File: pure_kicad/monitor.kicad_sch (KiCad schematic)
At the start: 46 parts, among them J3 XT60M, J4 XT60M, J5 Conn_01x04_Pin, J6 Conn_01x04_Pin, Q5 Q_PMOS_SGD, Q6 Q_NMOS_DGS, Q7 Q_NMOS_DGS, U2 BQ40Z80RSMR

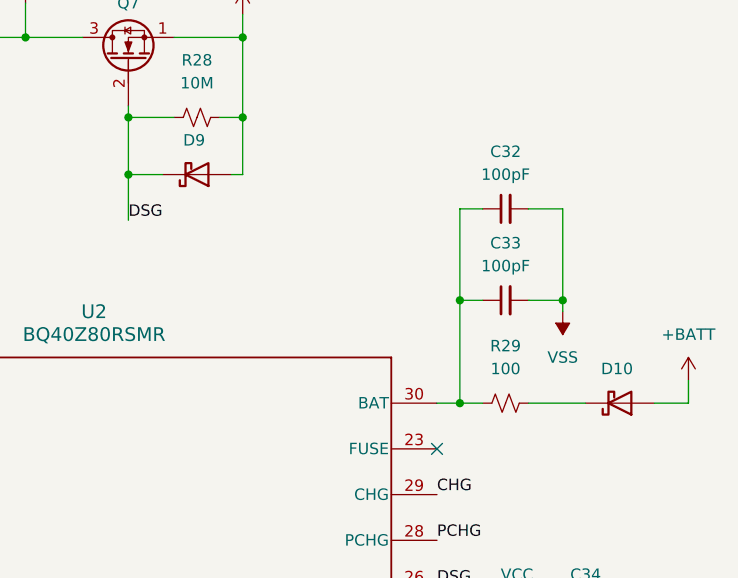
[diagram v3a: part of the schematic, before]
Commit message: So, 10u X5Rs are a thing. Just use 40 of them
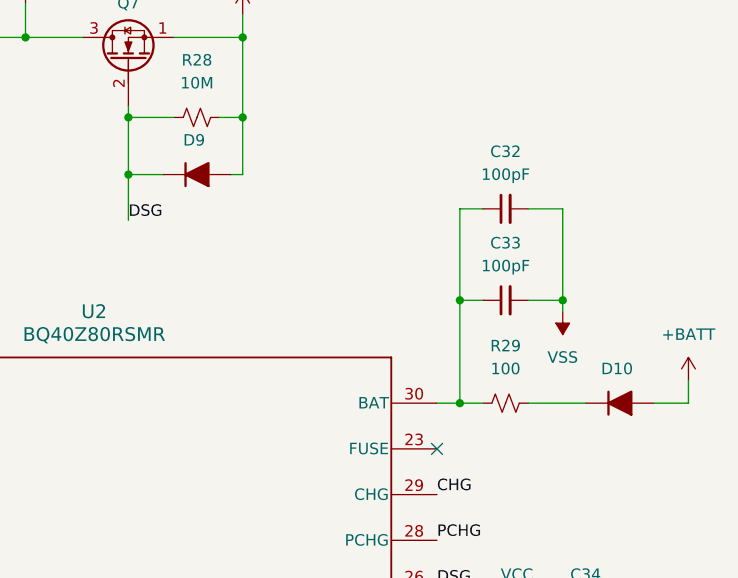
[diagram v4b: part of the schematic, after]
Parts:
- D10, D9: value D_Schottky -> 1N4001; footprint cyberec:D_SMA_Handsoldering -> cyberec:D_SOD-123F; symbol Device:D_Schottky -> Device:D_Filled
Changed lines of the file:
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@@
 	)
 	(symbol
-		(lib_id "Device:D_Schottky")
+		(lib_id "Device:D_Filled")
 		(at 173.99 48.26 0)
 		(mirror x)
@@
 			)
 		)
-		(property "Value" "D_Schottky"
+		(property "Value" "1N4001"
 			(at 173.6725 44.45 0)
 			(effects
@@
 			)
 		)
-		(property "Footprint" "cyberec:D_SMA_Handsoldering"
+		(property "Footprint" "cyberec:D_SOD-123F"
 			(at 173.99 48.26 0)
 			(effects
@@
 			)
 		)
-		(property "Description" "Schottky diode"
+		(property "Description" "Diode, filled shape"
+			(at 173.99 48.26 0)
+			(effects
+				(font
+					(size 1.27 1.27)
+				)
+				(hide yes)
+			)
+		)
+		(property "Sim.Device" "D"
+			(at 173.99 48.26 0)
+			(effects
+				(font
+					(size 1.27 1.27)
+				)
+				(hide yes)
+			)
+		)
+		(property "Sim.Pins" "1=K 2=A"
 			(at 173.99 48.26 0)
 			(effects
@@
 	)
 	(symbol
-		(lib_id "Device:D_Schottky")
+		(lib_id "Device:D_Filled")
 		(at 220.98 73.66 0)
 		(mirror x)
@@
 			)
 		)
-		(property "Value" "D_Schottky"
+		(property "Value" "1N4001"
 			(at 220.6625 69.85 0)
 			(effects
@@
 			)
 		)
-		(property "Footprint" "cyberec:D_SMA_Handsoldering"
+		(property "Footprint" "cyberec:D_SOD-123F"
 			(at 220.98 73.66 0)
 			(effects
@@
 			)
 		)
-		(property "Description" "Schottky diode"
-			(at 220.98 73.66 0)
-			(effects
+		(property "Description" "Diode, filled shape"
+			(at 220.98 73.66 0)
+			(effects
+				(font
+					(size 1.27 1.27)
+				)
+				(hide yes)
+			)
+		)
+		(property "Sim.Device" "D"
+			(at 220.98 73.66 0)
+			(effects
+				(font
+					(size 1.27 1.27)
+				)
+				(hide yes)
+			)
+		)
+		(property "Sim.Pins" "1=K 2=A"
+			(at 220.98 73.66 0)
+			(effects

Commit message: Layout is mostly good. Still need i2c and stuff
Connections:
- net +BATT: no longer D10.2 (A)
- net cell3: now reaches J5.4 (Pin_4), R23.2
- net cell6: now reaches J5.1 (Pin_1), R19.2
- net cell6: now also D10.2 (A)
- net cell5: now reaches J5.2 (Pin_2), R20.2
- net cell4: now reaches J5.3 (Pin_3), R21.2
- net cell2: now reaches J6.2 (Pin_2), R24.2
- net cell1: now reaches J6.3 (Pin_3), R25.2
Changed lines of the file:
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@@
+		)
+	)
+	(label "cell3"
+		(at 35.56 111.76 0)
+		(effects
+			(font
+				(size 1.27 1.27)
+			)
+			(justify left bottom)
 		)
 	)
@@
 		)
 	)
+	(label "cell6"
+		(at 35.56 104.14 0)
+		(effects
+			(font
+				(size 1.27 1.27)
+			)
+			(justify left bottom)
+		)
+	)
 	(label "LED_C"
 		(at 95.25 179.07 180)
@@
 		)
 	)
+	(label "cell1"
+		(at 35.56 127 0)
+		(effects
+			(font
+				(size 1.27 1.27)
+			)
+			(justify left bottom)
+		)
+	)
 	(label "LED_B"
 		(at 95.25 171.45 180)
@@
 		)
 	)
+	(label "cell5"
+		(at 35.56 106.68 0)
+		(effects
+			(font
+				(size 1.27 1.27)
+			)
+			(justify left bottom)
+		)
+	)
 	(label "DSG"
 		(at 200.66 93.98 0)
@@
 		)
 	)
+	(label "cell6"
+		(at 228.6 71.12 0)
+		(effects
+			(font
+				(size 1.27 1.27)
+			)
+			(justify left bottom)
+		)
+	)
 	(label "SRP"
 		(at 124.46 101.6 180)
@@
 		)
 	)
+	(label "cell2"
+		(at 35.56 124.46 0)
+		(effects
+			(font
+				(size 1.27 1.27)
+			)
+			(justify left bottom)
+		)
+	)
 	(label "SRN"
 		(at 124.46 106.68 180)
@@
 	(label "CHG"
 		(at 144.78 49.53 0)
+		(effects
+			(font
+				(size 1.27 1.27)
+			)
+			(justify left bottom)
+		)
+	)
+	(label "cell4"
+		(at 35.56 109.22 0)
 		(effects
 			(font
@@
 					(unit 1)
 				)
-			)
-		)
-	)
-	(symbol
-		(lib_id "power:+BATT")
-		(at 228.6 71.12 0)
-		(unit 1)
-		(exclude_from_sim no)
-		(in_bom yes)
-		(on_board yes)
-		(dnp no)
-		(fields_autoplaced yes)
-		(property "Reference" "#PWR056"
-			(at 228.6 74.93 0)
-			(effects
-				(font
-					(size 1.27 1.27)
-				)
-				(hide yes)
-			)
-		)
-		(property "Value" "+BATT"
-			(at 228.6 66.04 0)
-			(effects
-				(font
-					(size 1.27 1.27)
-				)
-			)
-		)
-		(property "Footprint" ""
-			(at 228.6 71.12 0)
-			(effects
-				(font
-					(size 1.27 1.27)
-				)
-				(hide yes)
-			)
-		)
-		(property "Datasheet" ""
-			(at 228.6 71.12 0)
-			(effects
-				(font
-					(size 1.27 1.27)
-				)
-				(hide yes)
-			)
-		)
-		(property "Description" "Power symbol creates a global label with name \"+BATT\""
-			(at 228.6 71.12 0)
-			(effects
-				(font
-					(size 1.27 1.27)
-				)
-				(hide yes)
-			)
-		)
-		(pin "1"
-		)
-		(instances
-			(project "cyberec"
-				(path "/40353889-c50f-4e31-a1c9-0677743efa04/8b99ca33-10b1-4de7-aaf1-12ec8d8c3fec"
-					(reference "#PWR056")
-					(unit 1)
-				)

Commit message: I think this was just sorting LEDs
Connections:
- net -BATT: now also C34.1; no longer C34.2
- net VCC: now also C34.2; no longer C34.1
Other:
- moved on the sheet: C34
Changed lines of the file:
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@@
 	(symbol
 		(lib_id "Device:C_Small")
-		(at 217.17 99.06 90)
+		(at 217.17 99.06 270)
+		(mirror x)
 		(unit 1)
 		(exclude_from_sim no)
@@
 		(on_board yes)
 		(dnp no)
-		(fields_autoplaced yes)
 		(property "Reference" "C34"
-			(at 217.1763 92.71 90)
+			(at 217.1637 92.71 90)
 			(effects
 				(font
@@
 		)
 		(property "Value" "100nF"
-			(at 217.1763 95.25 90)
+			(at 217.1637 95.25 90)
 			(effects
 				(font

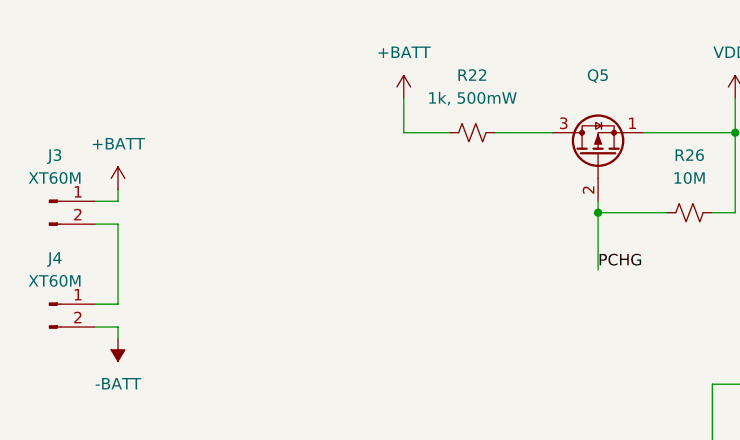
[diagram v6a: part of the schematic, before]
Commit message: Re-layout top side. Bottom to follow
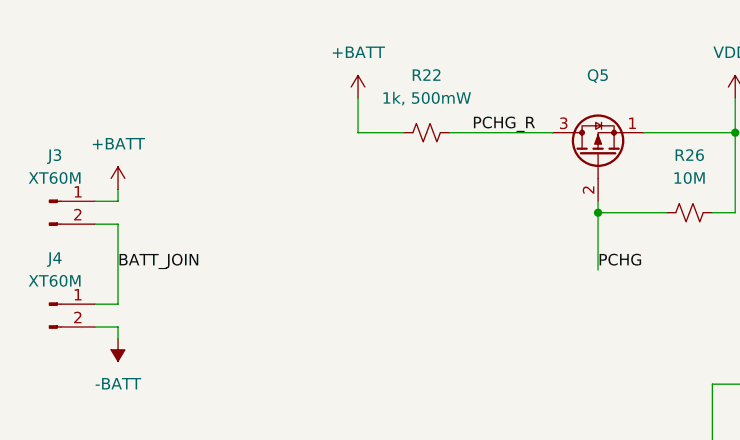
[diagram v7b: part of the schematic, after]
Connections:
- net PCHG_R: now reaches Q5.3 (D), R22.1
- net BATT_JOIN: now reaches J3.2 (Pin_2), J4.1 (Pin_1)
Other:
- moved on the sheet: R22
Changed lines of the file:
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@@
 	(wire
 		(pts
-			(xy 80.01 35.56) (xy 86.36 35.56)
+			(xy 74.93 35.56) (xy 86.36 35.56)
 		)
 		(stroke
@@
 	(wire
 		(pts
-			(xy 69.85 35.56) (xy 74.93 35.56)
+			(xy 64.77 35.56) (xy 69.85 35.56)
 		)
 		(stroke
@@
 	(wire
 		(pts
-			(xy 69.85 31.75) (xy 69.85 35.56)
+			(xy 64.77 31.75) (xy 64.77 35.56)
 		)
 		(stroke
@@
 		)
 	)
+	(label "BATT_JOIN"
+		(at 38.1 50.8 0)
+		(effects
+			(font
+				(size 1.27 1.27)
+			)
+			(justify left bottom)
+		)
+	)
 	(label "cell2"
 		(at 35.56 124.46 0)
@@
 		)
 	)
+	(label "PCHG_R"
+		(at 77.47 35.56 0)
+		(effects
+			(font
+				(size 1.27 1.27)
+			)
+			(justify left bottom)
+		)
+	)
 	(label "cell4"
 		(at 35.56 109.22 0)
@@
 	(symbol
 		(lib_id "Device:R_Small_US")
-		(at 77.47 35.56 270)
+		(at 72.39 35.56 270)
 		(unit 1)
 		(exclude_from_sim no)
@@
 		(fields_autoplaced yes)
 		(property "Reference" "R22"
-			(at 77.47 29.21 90)
+			(at 72.39 29.21 90)
 			(effects
 				(font
@@
 		)
 		(property "Value" "1k, 500mW"
-			(at 77.47 31.75 90)
+			(at 72.39 31.75 90)
 			(effects
 				(font
@@
 		)
 		(property "Footprint" "cyberec:R_1210_3225Metric_Pad1.30x2.65mm_HandSolder"
-			(at 77.47 35.56 0)
+			(at 72.39 35.56 0)
 			(effects
 				(font
@@
 		)
 		(property "Datasheet" "~"
-			(at 77.47 35.56 0)
+			(at 72.39 35.56 0)
 			(effects
 				(font
@@
 		)
 		(property "Description" "Resistor, small US symbol"
-			(at 77.47 35.56 0)
+			(at 72.39 35.56 0)
 			(effects
 				(font
@@
 	(symbol
 		(lib_id "power:+BATT")
-		(at 69.85 31.75 0)
+		(at 64.77 31.75 0)
 		(unit 1)
 		(exclude_from_sim no)
@@
 		(fields_autoplaced yes)
 		(property "Reference" "#PWR043"
-			(at 69.85 35.56 0)
+			(at 64.77 35.56 0)
 			(effects
 				(font
@@
 		)
 		(property "Value" "+BATT"
-			(at 69.85 26.67 0)
+			(at 64.77 26.67 0)
 			(effects
 				(font
@@
 		)
 		(property "Footprint" ""
-			(at 69.85 31.75 0)
+			(at 64.77 31.75 0)
 			(effects
 				(font
@@
 		)
 		(property "Datasheet" ""
-			(at 69.85 31.75 0)
+			(at 64.77 31.75 0)
 			(effects
 				(font
@@
 		)
 		(property "Description" "Power symbol creates a global label with name \"+BATT\""
-			(at 69.85 31.75 0)
+			(at 64.77 31.75 0)
 			(effects
 				(font

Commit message: I think the routing so far is done. I've started collecting signals to route off the board
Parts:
- added J7: Pack Thermistor 1, Connector_PinHeader_2.00mm:PinHeader_1x02_P2.00mm_Vertical, symbol Connector_Generic:Conn_01x02
- added J8: Pack Thermistor 2, Connector_PinHeader_2.00mm:PinHeader_1x02_P2.00mm_Vertical, symbol Connector_Generic:Conn_01x02
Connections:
- net -BATT: now also J7.2 (Pin_2), J8.2 (Pin_2)
- net TS_PACK1: now also J7.1 (Pin_1)
- net TS_PACK2: now also J8.1 (Pin_1)
- net nDISP: now reaches U2.15 (DISP_GPIO_N)
- net PDSG: now reaches U2.16 (PDSG_GPIO)
- net nPRES: now reaches U2.17 (PRES_SHUTDOWN_DISP_PDSG_GPIO_N)
- net BATT_JOIN: no longer names the net of J3.2 (Pin_2), J4.1 (Pin_1)
- net PCHG_R: no longer names the net of Q5.3 (D), R22.1
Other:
- moved on the sheet: R22
